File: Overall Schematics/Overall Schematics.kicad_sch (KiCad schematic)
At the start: 37 parts, among them J1 WattMeter1_Output, J2 WattMeter2_Output, J3 Intel_Buck_Converter_Input, J4 WattMeter1_Input, J5 WattMeter2_Input, M1 Stepper_Motor_bipolar, M10 Motor_Servo, M11 Stepper_Motor_bipolar, M12 Motor_Servo, M2 Stepper_Motor_bipolar, M3 LinActuator12V, M4 LinActuator12V, M5 LinActuator12V, M6 Motor_DC, M7 Motor_DC, M8 Motor_DC, M9 Motor_DC, SW1 SW_DPST, U1 Teensy4.1, U10 VNH52019, U11 ServoDriver, U12 36v4SMD, U13 D24V22F5, U2 36v4SMD, U3 36v4SMD, U4 VNH52019, U5 VNH52019, U6 VNH52019, U7 VNH52019, U8 VNH52019, U9 VNH52019

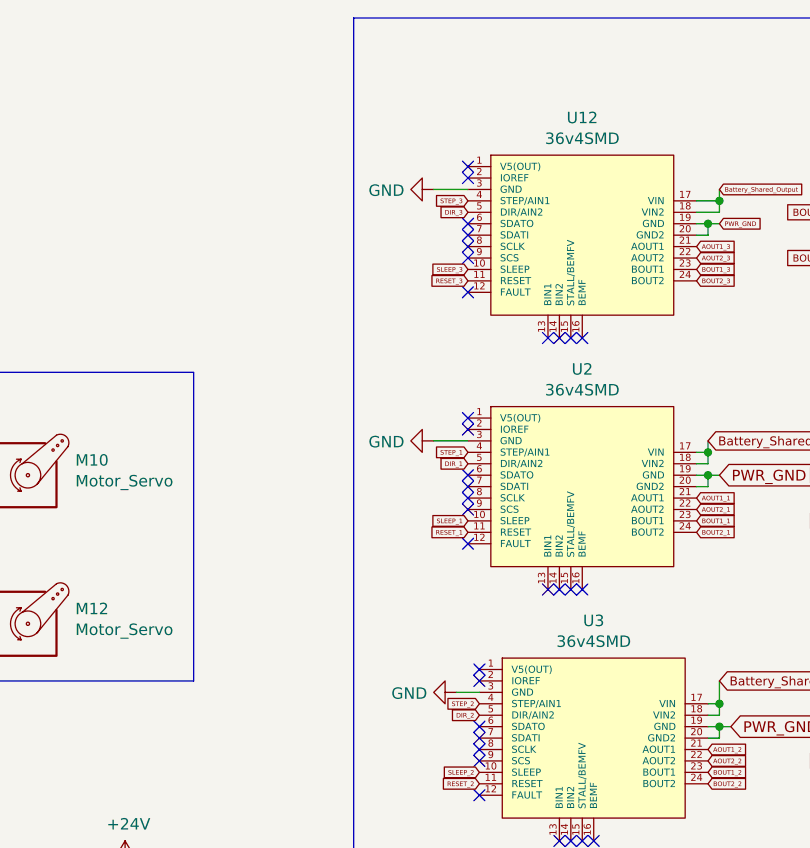
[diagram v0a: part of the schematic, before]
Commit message: Schematic layout set needs routing
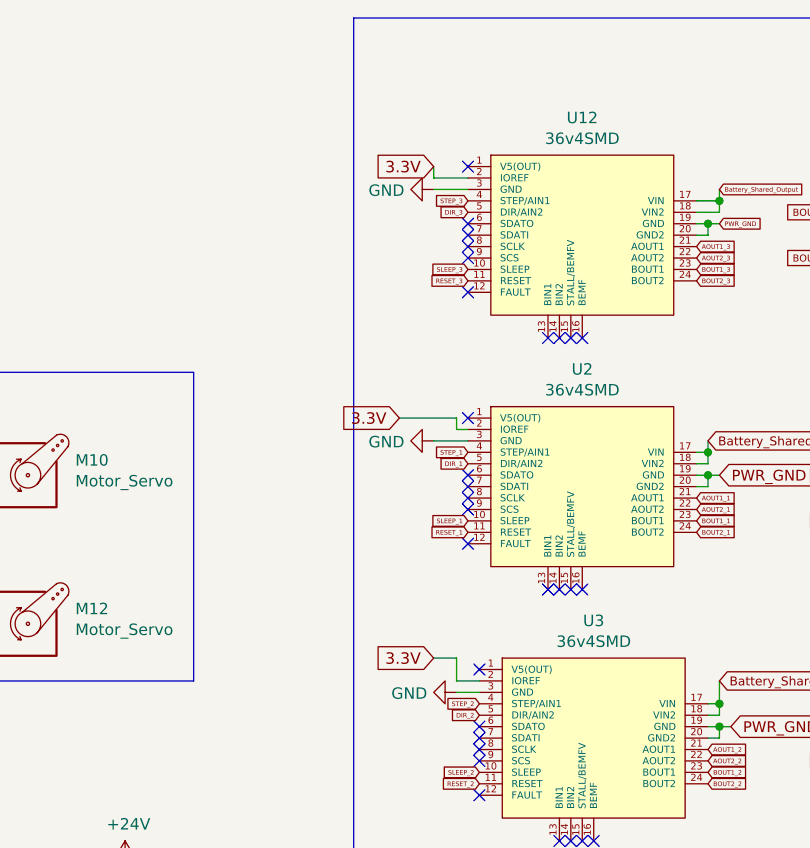
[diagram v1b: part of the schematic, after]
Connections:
- net +3V3: now also U12.2 (IOREF), U2.2 (IOREF), U3.2 (IOREF)
- no-connect marks 102 -> 99
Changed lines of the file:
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@@
   (junction (at 740.41 354.33) (diameter 0) (color 0 0 0 0)
   )
-  (no_connect (at 571.5 266.7))
   (no_connect (at 572.77 293.37))
   (no_connect (at 698.5 405.13))
@@
   (no_connect (at 582.93 312.42))
   (no_connect (at 695.96 302.26))
-  (no_connect (at 572.77 294.64))
   (no_connect (at 476.25 383.54))
   (no_connect (at 502.92 274.32))
@@
   (no_connect (at 695.96 325.12))
   (no_connect (at 571.5 274.32))
-  (no_connect (at 571.5 238.76))
   (no_connect (at 572.77 421.64))
   (no_connect (at 695.96 265.43))
@@
     (stroke (width 0) (type default) (color 0 0 0 0))
   )
+  (wire (pts (xy 567.69 238.76) (xy 567.69 237.49))
+    (stroke (width 0) (type default) (color 0 0 0 0))
+  )
   (wire (pts (xy 598.17 270.51) (xy 598.17 269.24))
     (stroke (width 0) (type default) (color 0 0 0 0))
@@
     (stroke (width 0) (type default) (color 0 0 0 0))
   )
+  (wire (pts (xy 563.88 265.43) (xy 570.23 265.43))
+    (stroke (width 0) (type default) (color 0 0 0 0))
+  )
   (wire (pts (xy 599.44 393.7) (xy 601.98 393.7))
     (stroke (width 0) (type default) (color 0 0 0 0))
@@
     (stroke (width 0) (type default) (color 0 0 0 0))
   )
+  (wire (pts (xy 570.23 266.7) (xy 571.5 266.7))
+    (stroke (width 0) (type default) (color 0 0 0 0))
+  )
   (wire (pts (xy 510.54 283.21) (xy 510.54 274.32))
     (stroke (width 0) (type default) (color 0 0 0 0))
@@
     (stroke (width 0) (type default) (color 0 0 0 0))
   )
+  (wire (pts (xy 572.77 294.64) (xy 570.23 294.64))
+    (stroke (width 0) (type default) (color 0 0 0 0))
+  )
   (wire (pts (xy 599.44 300.99) (xy 599.44 299.72))
     (stroke (width 0) (type default) (color 0 0 0 0))
@@
     (stroke (width 0) (type default) (color 0 0 0 0))
   )
+  (wire (pts (xy 570.23 294.64) (xy 570.23 292.1))
+    (stroke (width 0) (type default) (color 0 0 0 0))
+  )
   (wire (pts (xy 728.98 386.08) (xy 728.98 383.54))
     (stroke (width 0) (type default) (color 0 0 0 0))
@@
     (stroke (width 0) (type default) (color 0 0 0 0))
   )
+  (wire (pts (xy 567.69 238.76) (xy 571.5 238.76))
+    (stroke (width 0) (type default) (color 0 0 0 0))
+  )
   (wire (pts (xy 695.96 321.31) (xy 684.53 321.31))
     (stroke (width 0) (type default) (color 0 0 0 0))
@@
     (stroke (width 0) (type default) (color 0 0 0 0))
   )
+  (wire (pts (xy 570.23 265.43) (xy 570.23 266.7))
+    (stroke (width 0) (type default) (color 0 0 0 0))
+  )
   (wire (pts (xy 598.17 391.16) (xy 599.44 391.16))
     (stroke (width 0) (type default) (color 0 0 0 0))
@@
   )
   (wire (pts (xy 637.54 364.49) (xy 635 364.49))
+    (stroke (width 0) (type default) (color 0 0 0 0))
+  )
+  (wire (pts (xy 567.69 292.1) (xy 570.23 292.1))
     (stroke (width 0) (type default) (color 0 0 0 0))
   )
@@
     )
   )
+  (global_label "3.3V" (shape input) (at 567.69 292.1 180) (fields_autoplaced)
+    (effects (font (size 1.27 1.27)) (justify right))
+    (property "Intersheet References" "${INTERSHEET_REFS}" (id 0) (at 1116.33 -33.02 0)
+      (effects (font (size 1.27 1.27)) (justify left) hide)
+    )
+  )
   (global_label "3.3V" (shape input) (at 684.53 299.72 180) (fields_autoplaced)
     (effects (font (size 1.27 1.27)) (justify right))
@@
     )
   )
+  (global_label "3.3V" (shape input) (at 563.88 265.43 180) (fields_autoplaced)
+    (effects (font (size 1.27 1.27)) (justify right))
+    (property "Intersheet References" "${INTERSHEET_REFS}" (id 0) (at 1112.52 -59.69 0)
+      (effects (font (size 1.27 1.27)) (justify left) hide)
+    )
+  )
   (global_label "OUTB2_LIN" (shape input) (at 633.73 398.78 270) (fields_autoplaced)
     (effects (font (size 0.508 0.508)) (justify right))
@@
     )
   )
+  (global_label "3.3V" (shape input) (at 567.69 237.49 180) (fields_autoplaced)
+    (effects (font (size 1.27 1.27)) (justify right))
+    (property "Intersheet References" "${INTERSHEET_REFS}" (id 0) (at 1116.33 -87.63 0)
+      (effects (font (size 1.27 1.27)) (justify left) hide)
+    )
+  )

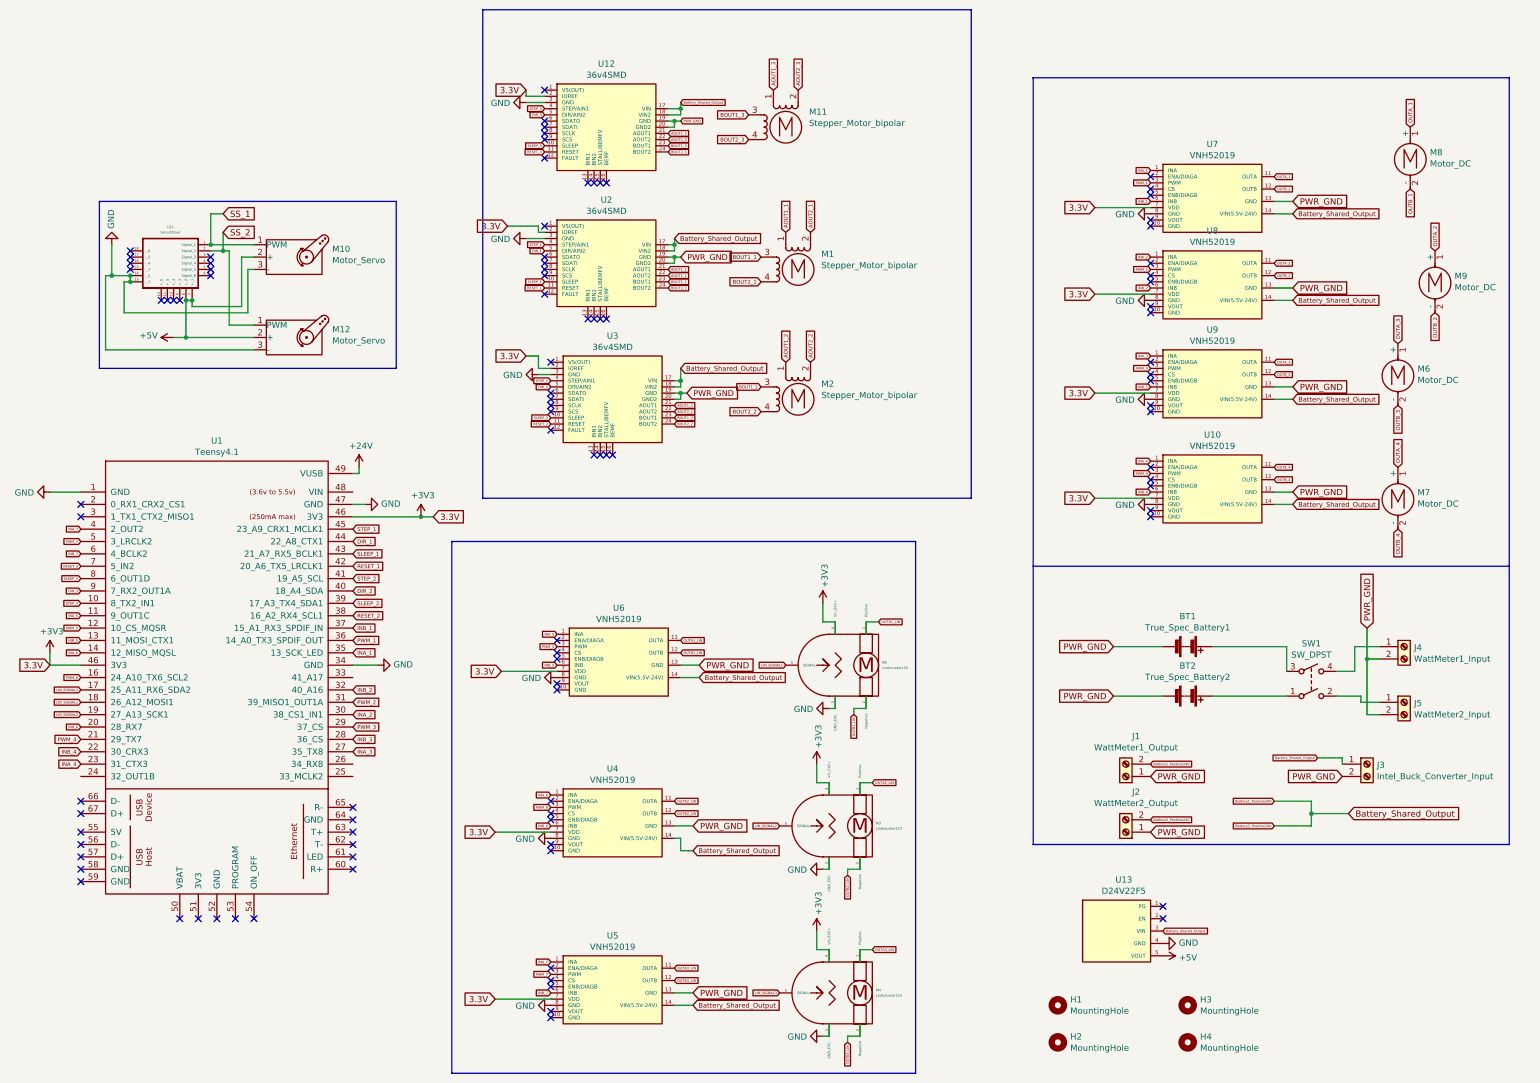
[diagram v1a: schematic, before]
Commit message: 4-Layer Setup
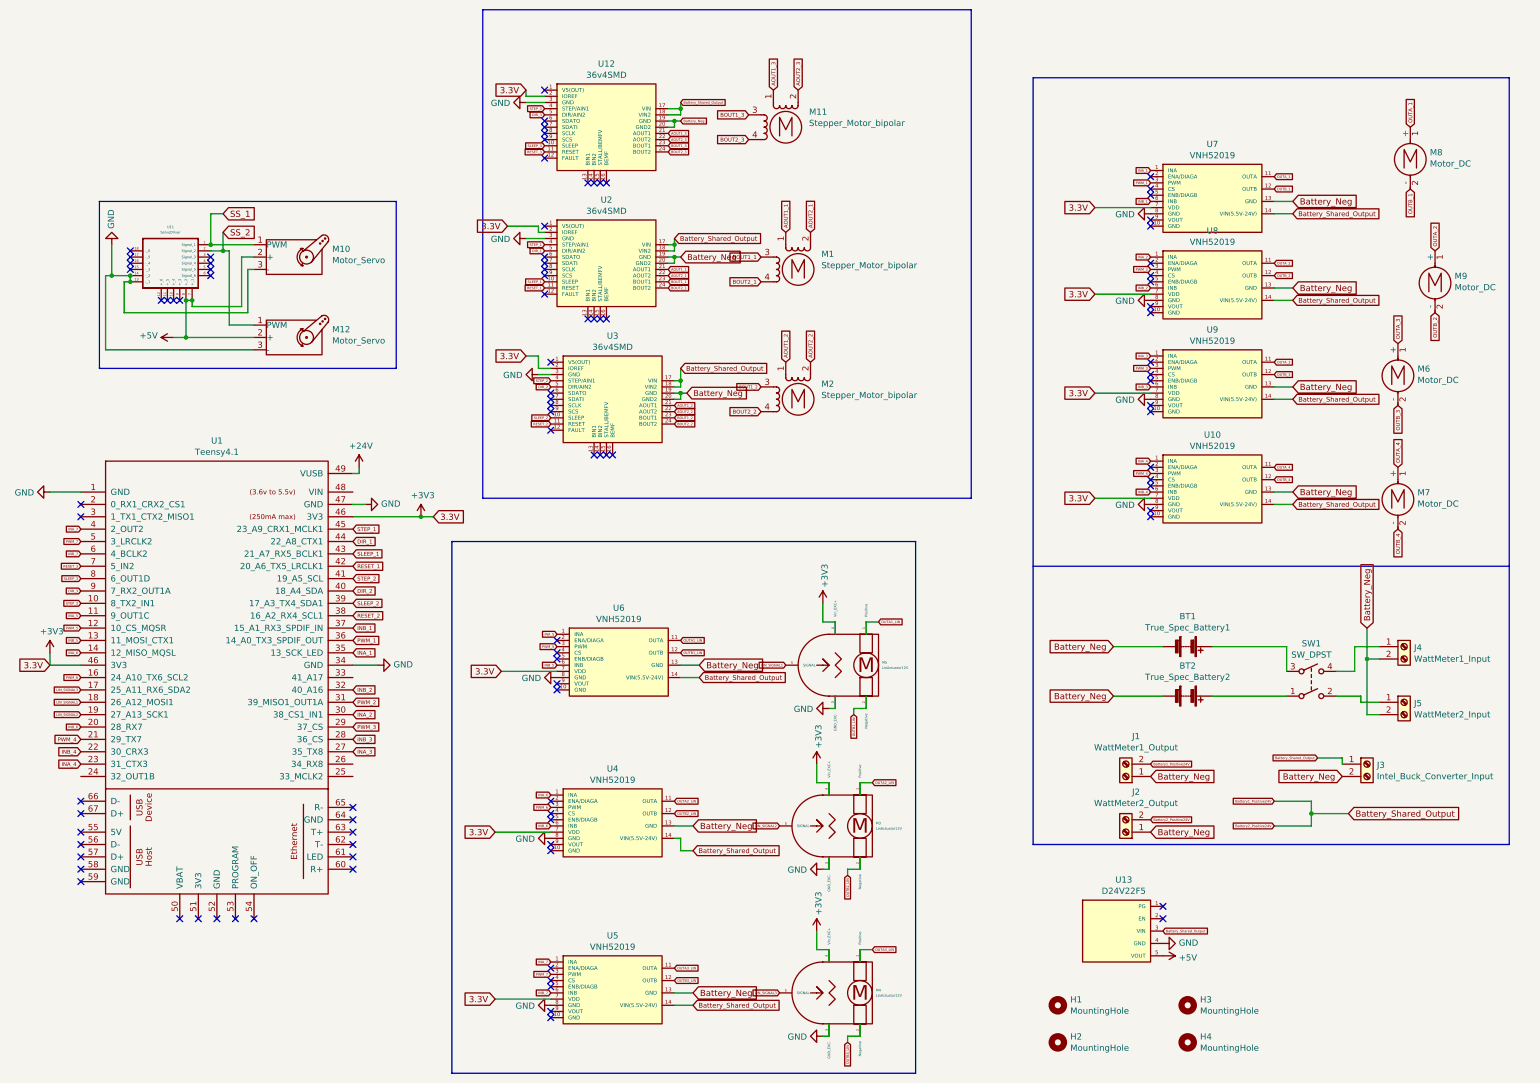
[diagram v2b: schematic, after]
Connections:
- net PWR_GND renamed Battery_Neg
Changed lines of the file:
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@@
     )
   )
-  (global_label "PWR_GND" (shape input) (at 725.17 298.45 0) (fields_autoplaced)
+  (global_label "Battery_Neg" (shape input) (at 725.17 298.45 0) (fields_autoplaced)
     (effects (font (size 1.27 1.27)) (justify left))
     (property "Intersheet References" "${INTERSHEET_REFS}" (id 0) (at 0 0 0)
@@
     )
   )
-  (global_label "PWR_GND" (shape input) (at 688.34 351.79 180) (fields_autoplaced)
+  (global_label "Battery_Neg" (shape input) (at 688.34 351.79 180) (fields_autoplaced)
     (effects (font (size 1.27 1.27)) (justify right))
     (property "Intersheet References" "${INTERSHEET_REFS}" (id 0) (at 0 0 0)
@@
     )
   )
-  (global_label "PWR_GND" (shape input) (at 601.98 422.91 0) (fields_autoplaced)
-    (effects (font (size 1.27 1.27)) (justify left))
-    (property "Intersheet References" "${INTERSHEET_REFS}" (id 0) (at 0 0 0)
-      (effects (font (size 1.27 1.27)) hide)
-    )
-  )
-  (global_label "PWR_GND" (shape input) (at 735.33 378.46 180) (fields_autoplaced)
+  (global_label "Battery_Neg" (shape input) (at 601.98 422.91 0) (fields_autoplaced)
+    (effects (font (size 1.27 1.27)) (justify left))
+    (property "Intersheet References" "${INTERSHEET_REFS}" (id 0) (at 0 0 0)
+      (effects (font (size 1.27 1.27)) hide)
+    )
+  )
+  (global_label "Battery_Neg" (shape input) (at 735.33 378.46 180) (fields_autoplaced)
     (effects (font (size 1.27 1.27)) (justify right))
     (property "Intersheet References" "${INTERSHEET_REFS}" (id 0) (at 0 0 0)
@@
     )
   )
-  (global_label "PWR_GND" (shape input) (at 688.34 361.95 180) (fields_autoplaced)
+  (global_label "Battery_Neg" (shape input) (at 688.34 361.95 180) (fields_autoplaced)
     (effects (font (size 1.27 1.27)) (justify right))
     (property "Intersheet References" "${INTERSHEET_REFS}" (id 0) (at 0 0 0)
@@
     )
   )
-  (global_label "PWR_GND" (shape input) (at 695.96 389.89 0) (fields_autoplaced)
+  (global_label "Battery_Neg" (shape input) (at 695.96 389.89 0) (fields_autoplaced)
     (effects (font (size 1.27 1.27)) (justify left))
     (property "Intersheet References" "${INTERSHEET_REFS}" (id 0) (at 0 0 0)
@@
     )
   )
-  (global_label "PWR_GND" (shape input) (at 725.17 260.35 0) (fields_autoplaced)
+  (global_label "Battery_Neg" (shape input) (at 725.17 260.35 0) (fields_autoplaced)
     (effects (font (size 1.27 1.27)) (justify left))
     (property "Intersheet References" "${INTERSHEET_REFS}" (id 0) (at 0 0 0)
@@
     )
   )
-  (global_label "PWR_GND" (shape input) (at 740.41 347.98 90) (fields_autoplaced)
+  (global_label "Battery_Neg" (shape input) (at 740.41 347.98 90) (fields_autoplaced)
     (effects (font (size 1.27 1.27)) (justify left))
     (property "Intersheet References" "${INTERSHEET_REFS}" (id 0) (at 0 0 0)
@@
     )
   )
-  (global_label "PWR_GND" (shape input) (at 601.98 388.62 0) (fields_autoplaced)
+  (global_label "Battery_Neg" (shape input) (at 601.98 388.62 0) (fields_autoplaced)
     (effects (font (size 1.27 1.27)) (justify left))
     (property "Intersheet References" "${INTERSHEET_REFS}" (id 0) (at 0 0 0)
@@
     )
   )
-  (global_label "PWR_GND" (shape input) (at 695.96 378.46 0) (fields_autoplaced)
+  (global_label "Battery_Neg" (shape input) (at 695.96 378.46 0) (fields_autoplaced)
     (effects (font (size 1.27 1.27)) (justify left))
     (property "Intersheet References" "${INTERSHEET_REFS}" (id 0) (at 0 0 0)
@@
     )
   )
-  (global_label "PWR_GND" (shape input) (at 725.17 320.04 0) (fields_autoplaced)
+  (global_label "Battery_Neg" (shape input) (at 725.17 320.04 0) (fields_autoplaced)
     (effects (font (size 1.27 1.27)) (justify left))
     (property "Intersheet References" "${INTERSHEET_REFS}" (id 0) (at 0 0 0)
@@
     )
   )
-  (global_label "PWR_GND" (shape input) (at 599.44 271.78 0) (fields_autoplaced)
+  (global_label "Battery_Neg" (shape input) (at 599.44 271.78 0) (fields_autoplaced)
     (effects (font (size 1.1938 1.1938)) (justify left))
     (property "Intersheet References" "${INTERSHEET_REFS}" (id 0) (at 0 0 0)
@@
     )
   )
-  (global_label "PWR_GND" (shape input) (at 600.71 299.72 0) (fields_autoplaced)
+  (global_label "Battery_Neg" (shape input) (at 600.71 299.72 0) (fields_autoplaced)
     (effects (font (size 1.1938 1.1938)) (justify left))
     (property "Intersheet References" "${INTERSHEET_REFS}" (id 0) (at 0 0 0)
@@
     )
   )
-  (global_label "PWR_GND" (shape input) (at 603.25 355.6 0) (fields_autoplaced)
+  (global_label "Battery_Neg" (shape input) (at 603.25 355.6 0) (fields_autoplaced)
     (effects (font (size 1.27 1.27)) (justify left))
     (property "Intersheet References" "${INTERSHEET_REFS}" (id 0) (at 0 0 0)
@@
     )
   )
-  (global_label "PWR_GND" (shape input) (at 599.44 243.84 0) (fields_autoplaced)
+  (global_label "Battery_Neg" (shape input) (at 599.44 243.84 0) (fields_autoplaced)
     (effects (font (size 0.508 0.508)) (justify left))
     (property "Intersheet References" "${INTERSHEET_REFS}" (id 0) (at 0 0 0)
@@
     )
   )
-  (global_label "PWR_GND" (shape input) (at 725.17 278.13 0) (fields_autoplaced)
-    (effects (font (size 1.27 1.27)) (justify left))
-    (property "Intersheet References" "${INTERSHEET_REFS}" (id 0) (at 0 0 0)
+  (global_label "Battery_Neg" (shape input) (at 725.17 278.13 0) (fields_autoplaced)
+    (effects (font (size 1.27 1.27)) (justify left))
+    (property "Intersheet References" "${INTERSHEET_REFS}" (id 0) (at 0 0 0)
